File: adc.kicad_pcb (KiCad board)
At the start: 2 copper layers, 53.8 x 69.1 mm, 86 parts, among them J1 Conn_02x08_Odd_Even, J2 Conn_02x08_Odd_Even, J3 Conn_02x08_Odd_Even, J4 Conn_02x08_Odd_Even, J5 Conn_01x04_Male, J9 Conn_02x08_Odd_Even, U1 ADC128D818, U2 ADC128D818, U3 ADC128D818, U4 ADC128D818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

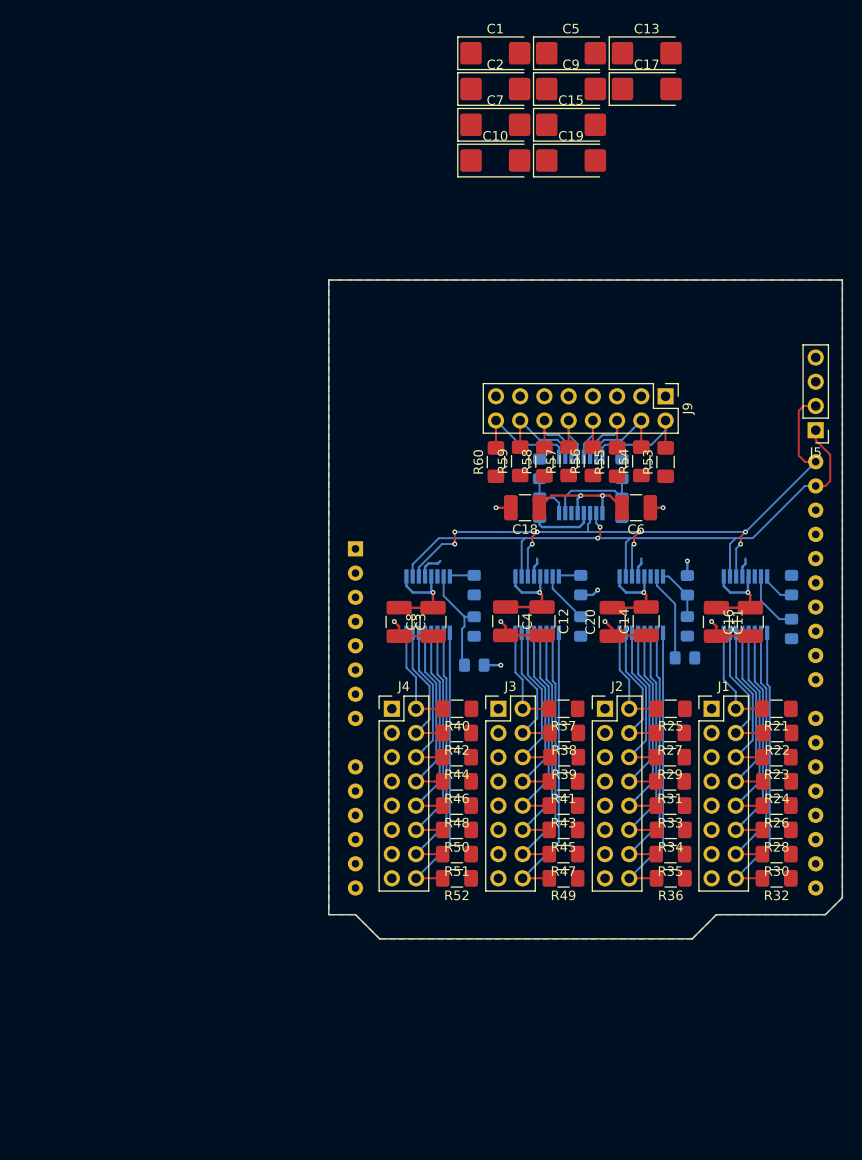
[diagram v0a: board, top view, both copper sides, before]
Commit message: add i2c pullup resistors
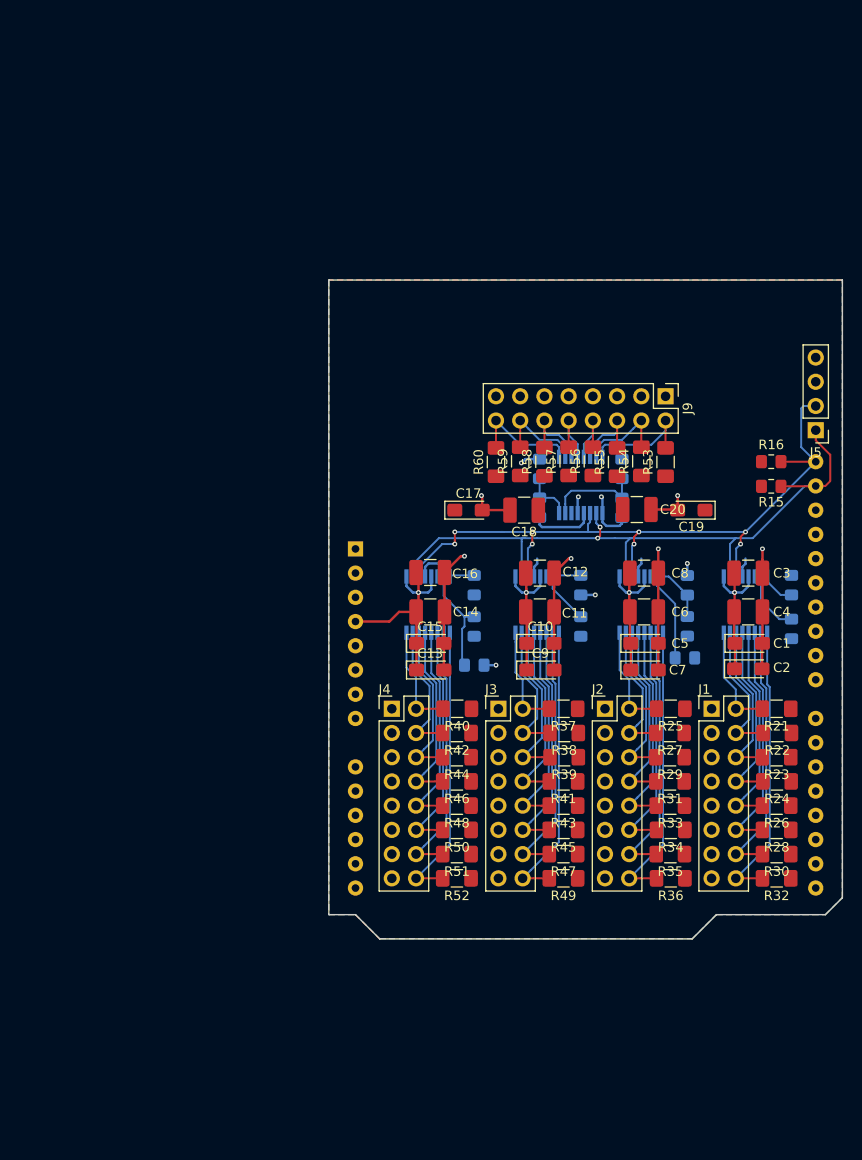
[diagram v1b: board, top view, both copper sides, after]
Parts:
- added R15: 1K, Resistor_SMD:R_0805_2012Metric_Pad1.15x1.40mm_HandSolder, F.Cu at (258.7, 101.6)
- added R16: 1K, Resistor_SMD:R_0805_2012Metric_Pad1.15x1.40mm_HandSolder, F.Cu at (258.7, 99.1)
- C1, C10, C13, C15, C17, C19, C2, C5, C7, C9: footprint Capacitor_Tantalum_SMD:CP_EIA-6032-28_Kemet-C_Pad2.25x2.35mm_HandSolder -> Capacitor_Tantalum_SMD:CP_EIA-3216-18_Kemet-A_Pad1.58x1.35mm_HandSolder
- moved C13 68.5 mm to (223.0, 120.9)
- moved C1 67.3 mm to (256.4, 118.1)
- moved C2 66.3 mm to (256.3, 120.8)
- moved C5 62.4 mm to (245.5, 118.1)
- moved C9 61.0 mm to (234.5, 120.9)
- moved C7 59.3 mm to (245.5, 120.9)
- moved C15 56.3 mm to (223.0, 118.1)
- moved C10 50.8 mm to (234.5, 118.1)
- moved C17 48.0 mm to (227.0, 104.1)
- moved C19 38.8 mm to (250.4, 104.1), turned to 180 degrees
- moved C3 37.0 mm to (256.3, 110.7), turned to 0 degrees
- moved C16 34.0 mm to (223.0, 110.7), turned to 180 degrees
- moved C4 25.5 mm to (256.3, 114.8), turned to 0 degrees
- moved C8 22.7 mm to (245.4, 110.7), turned to 180 degrees
- moved C14 22.7 mm to (223.0, 114.8), turned to 180 degrees
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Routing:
- net GND: track 40.0 -> 75.3 mm
- net 3V3: track 62.3 -> 82.2 mm, vias 9 -> 10
- net SDA: track 70.3 -> 73.9 mm
- net SCL: track 74.1 -> 76.6 mm

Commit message: silkscreen
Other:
- board text added: "3V3"
- board text added: "GND"
- board text added: "SCL"
- board text added: "SDA"

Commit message: PCBs ordered
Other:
- board text added: "1 | 0x1D"
- board text added: "2 | 0x1E"
- board text added: "3 | 0x1F"
- board text added: "4 | 0x2D"
- board text added: "5 | 0x2E"
- board text added: "ADC128D818 Thermistor Board Jacob Killelea"
- board text added: "CH 1"
- board text added: "CH 2"
- board text added: "CH 3"
- board text added: "CH 4"
- board text added: "CH 5"
- board text added: "CH | ADDR"

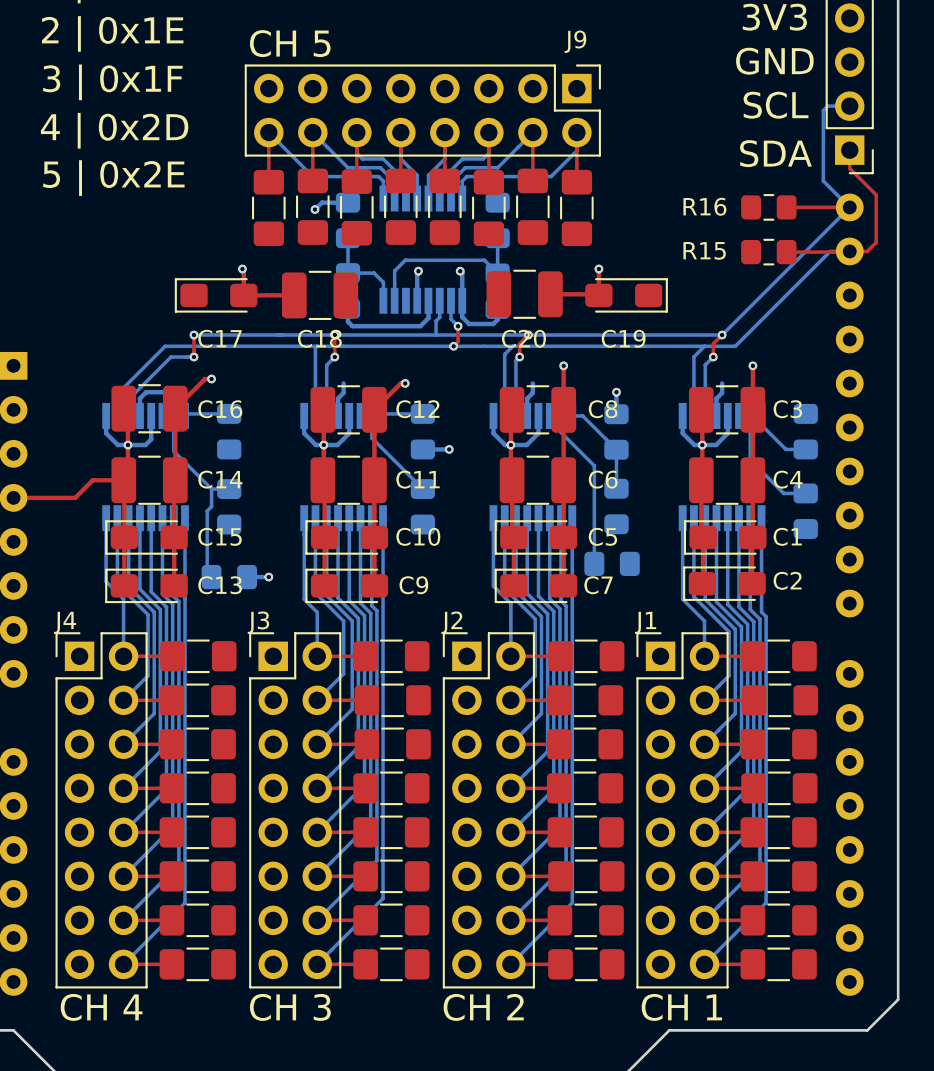
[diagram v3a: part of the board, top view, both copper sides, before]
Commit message: reroute with ITLL design rule tolerances. Switched this one to metric
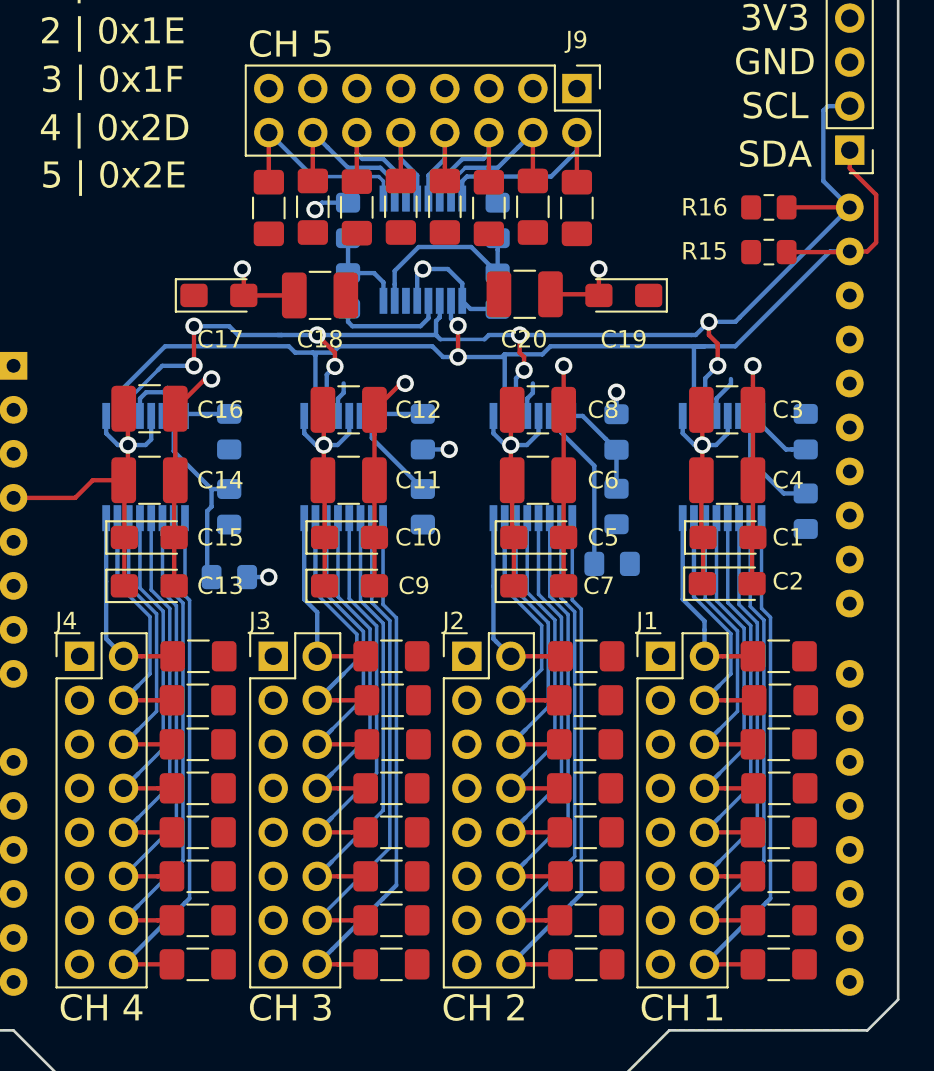
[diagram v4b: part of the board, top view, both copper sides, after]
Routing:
- net SCL: track 76.6 -> 79.8 mm
- net Net-(J3-Pad16): track 30.1 -> 30.8 mm
- net Net-(J3-Pad4): track 14.7 -> 15.3 mm
- net Net-(R13-Pad1): track 10.3 -> 10.9 mm
- net Net-(J3-Pad14): track 27.6 -> 28.2 mm
- net Net-(J3-Pad12): track 25.0 -> 25.6 mm
- net Net-(J3-Pad10): track 22.4 -> 23.0 mm
- net Net-(J3-Pad8): track 19.9 -> 20.4 mm
- net SDA: track 73.9 -> 74.4 mm
- net Net-(J3-Pad6): track 17.4 -> 17.9 mm
- net 3V3: track 82.2 -> 82.7 mm, vias 10 -> 9
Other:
- net class Default: clearance 0.1524 -> 0.1778; trace_width 0.2032 -> 0.254; via_dia 0.508 -> 1; via_drill 0.254 -> 0.6
- net class Power: clearance 0.1524 -> 0.1778; via_dia 0.508 -> 1; via_drill 0.254 -> 0.6
- rule trace_clearance: 0.1524 -> 0.1778
- rule via_min_size: 0.508 -> 0.6

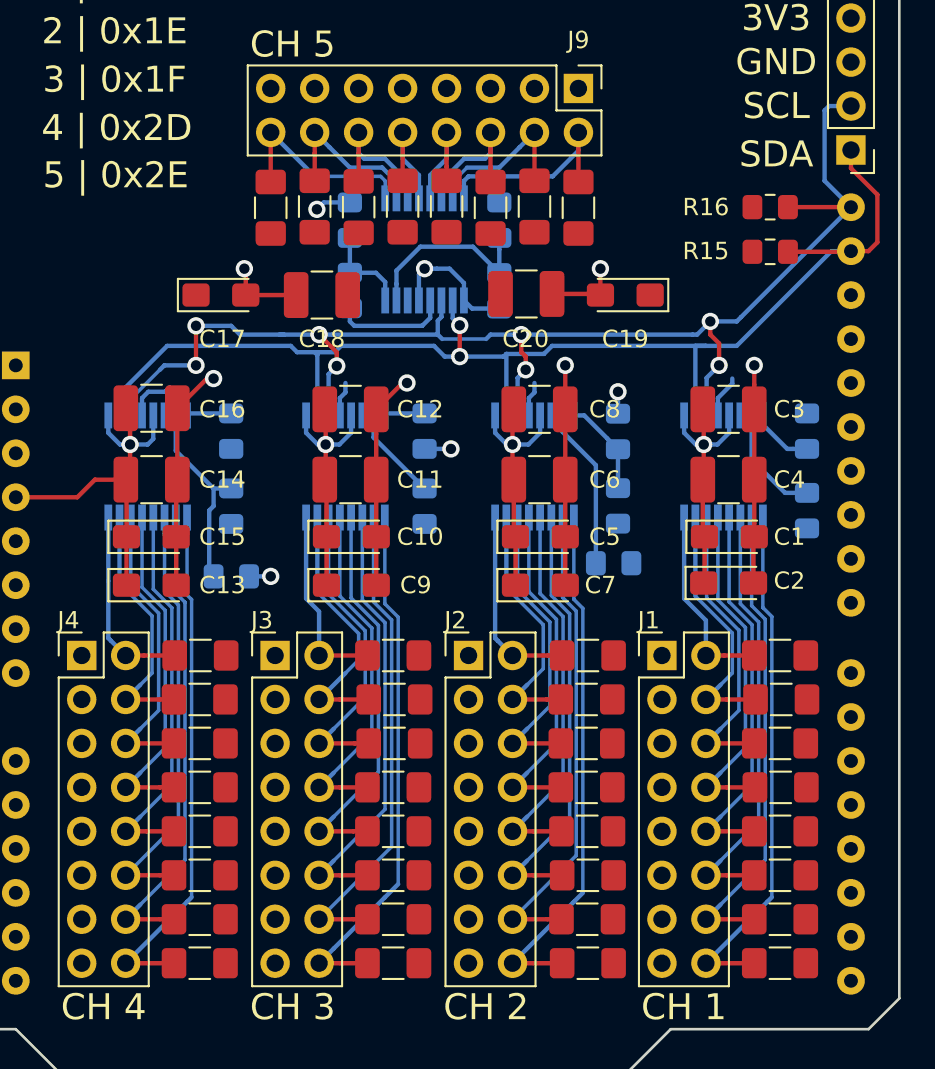
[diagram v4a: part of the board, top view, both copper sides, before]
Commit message: fix some remaining track widths
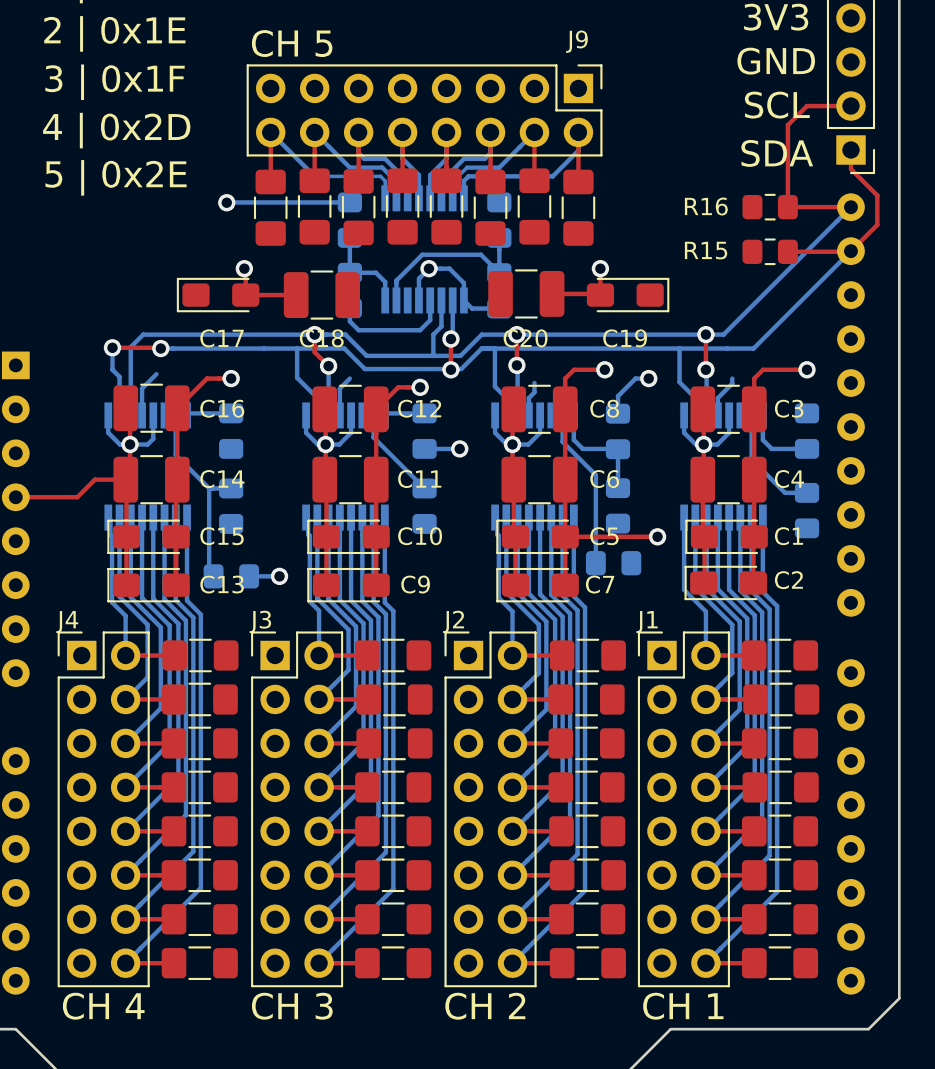
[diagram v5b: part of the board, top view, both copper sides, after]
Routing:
- net GND: track 75.8 -> 87.6 mm, vias 6 -> 7
- net 3V3: track 82.7 -> 90.6 mm
- net SDA: track 74.4 -> 78.4 mm, vias 2 -> 4
- net Net-(R3-Pad2): track 5.61 -> 6.44 mm
- net Net-(R13-Pad1): track 10.9 -> 10.2 mm
- net Net-(R1-Pad2): track 3.66 -> 4.18 mm
- net SCL: track 79.8 -> 80.2 mm, vias 8 -> 6

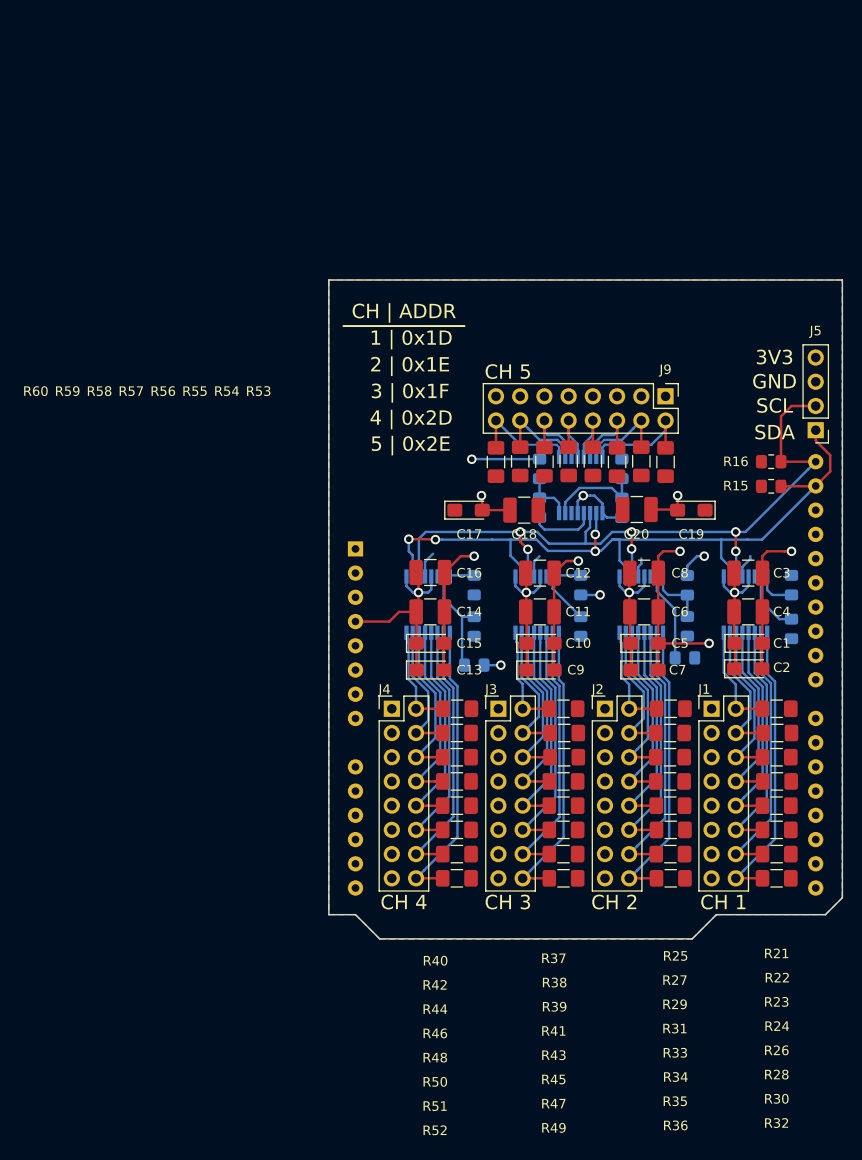
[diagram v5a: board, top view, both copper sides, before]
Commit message: update trace width after ITLL CNC cutting and correct error causing chip 0x1F to show up as 0x35
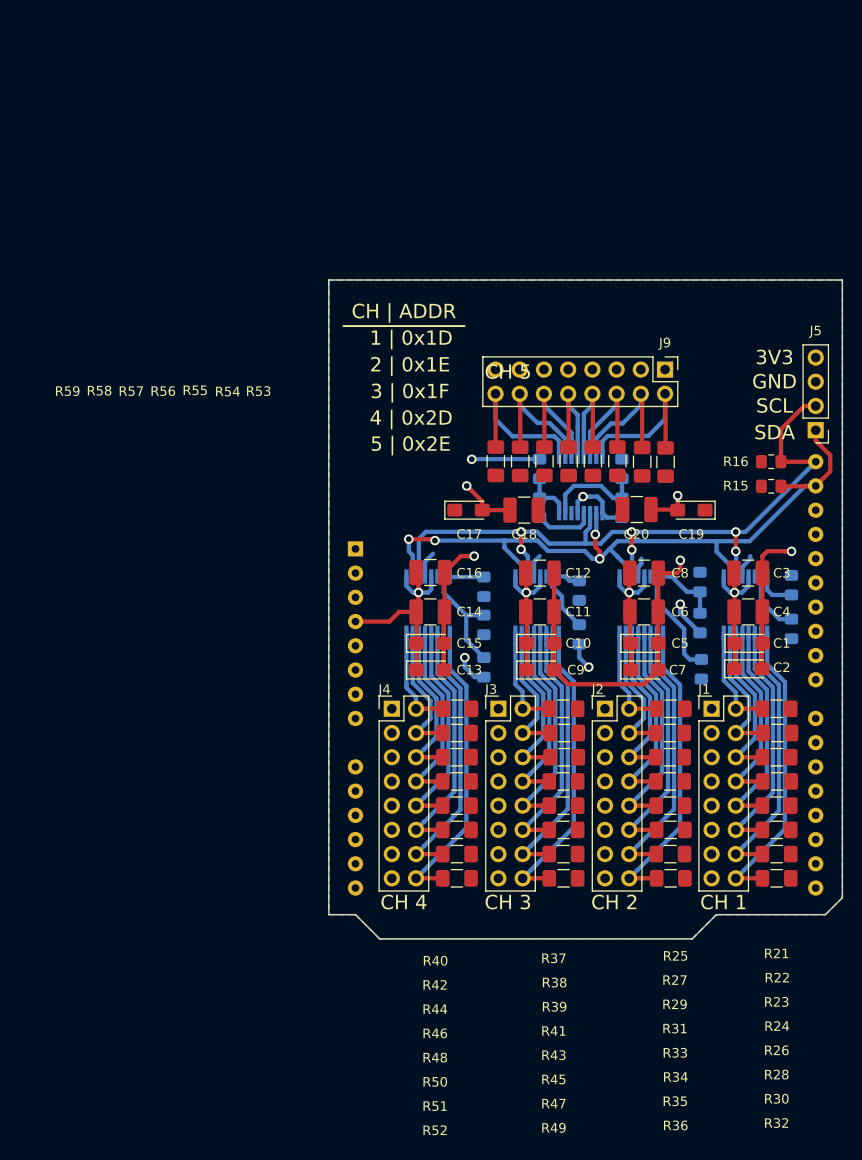
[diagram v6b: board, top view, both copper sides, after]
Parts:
- moved R6 5.17 mm to (238.6, 117.2)
- moved R3 4.83 mm to (251.3, 111.7), turned to 270 degrees
- moved R4 4.17 mm to (251.3, 116.0), turned to 270 degrees
- moved R7 3.77 mm to (238.6, 112.6)
- moved J9 2.80 mm to (247.6, 89.4)
- moved R5 2.09 mm to (251.4, 120.8), turned to 90 degrees
- moved R9 1.03 mm to (228.6, 120.6), turned to 270 degrees
- moved R8 1.03 mm to (228.6, 112.2)
- moved R10 1.03 mm to (228.6, 116.2)
- moved R54 0.10 mm to (245.2, 99.1)
- moved R55 0.09 mm to (242.6, 99.0)
- moved R60 0.09 mm to (229.8, 99.0)
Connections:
- U3 pad 7: Net-(R7-Pad2) -> Net-(R6-Pad1)
- U3 pad 8: Net-(R6-Pad1) -> Net-(R7-Pad2)
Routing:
- net Net-(J9-Pad16): track 11.6 -> 17.5 mm
- net Net-(J9-Pad10): track 7.00 -> 12.6 mm
- net Net-(J9-Pad8): track 7.00 -> 12.6 mm
- net Net-(J9-Pad14): track 9.66 -> 15.0 mm
- net Net-(J9-Pad4): track 9.66 -> 14.9 mm
- net Net-(J9-Pad2): track 12.3 -> 17.5 mm
- net Net-(J9-Pad12): track 8.52 -> 13.4 mm
- net Net-(J9-Pad6): track 8.56 -> 13.4 mm
- net GND: track 87.6 -> 91.5 mm, vias 7 -> 5
- net Net-(R6-Pad1): track 2.35 -> 6.21 mm
- net 3V3: track 90.6 -> 93.6 mm
- net Net-(R7-Pad2): track 5.44 -> 2.35 mm
- net Net-(R5-Pad2): track 9.33 -> 11.3 mm
- net Net-(R8-Pad2): track 2.60 -> 3.59 mm
- net Net-(J2-Pad16): track 30.6 -> 31.6 mm
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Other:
- net class Default: trace_width 0.254 -> 0.45
- net class Power: trace_width 0.254 -> 0.45
- board text added: "NOTE: ENSURE ALL DRILL HOLE SIZES ARE CORRECT FOR COMPONENT SHOULD BE APPROX 0.8 MM DIA"
